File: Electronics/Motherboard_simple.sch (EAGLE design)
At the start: 27 parts, among them U2 USD-SOCKETNEW

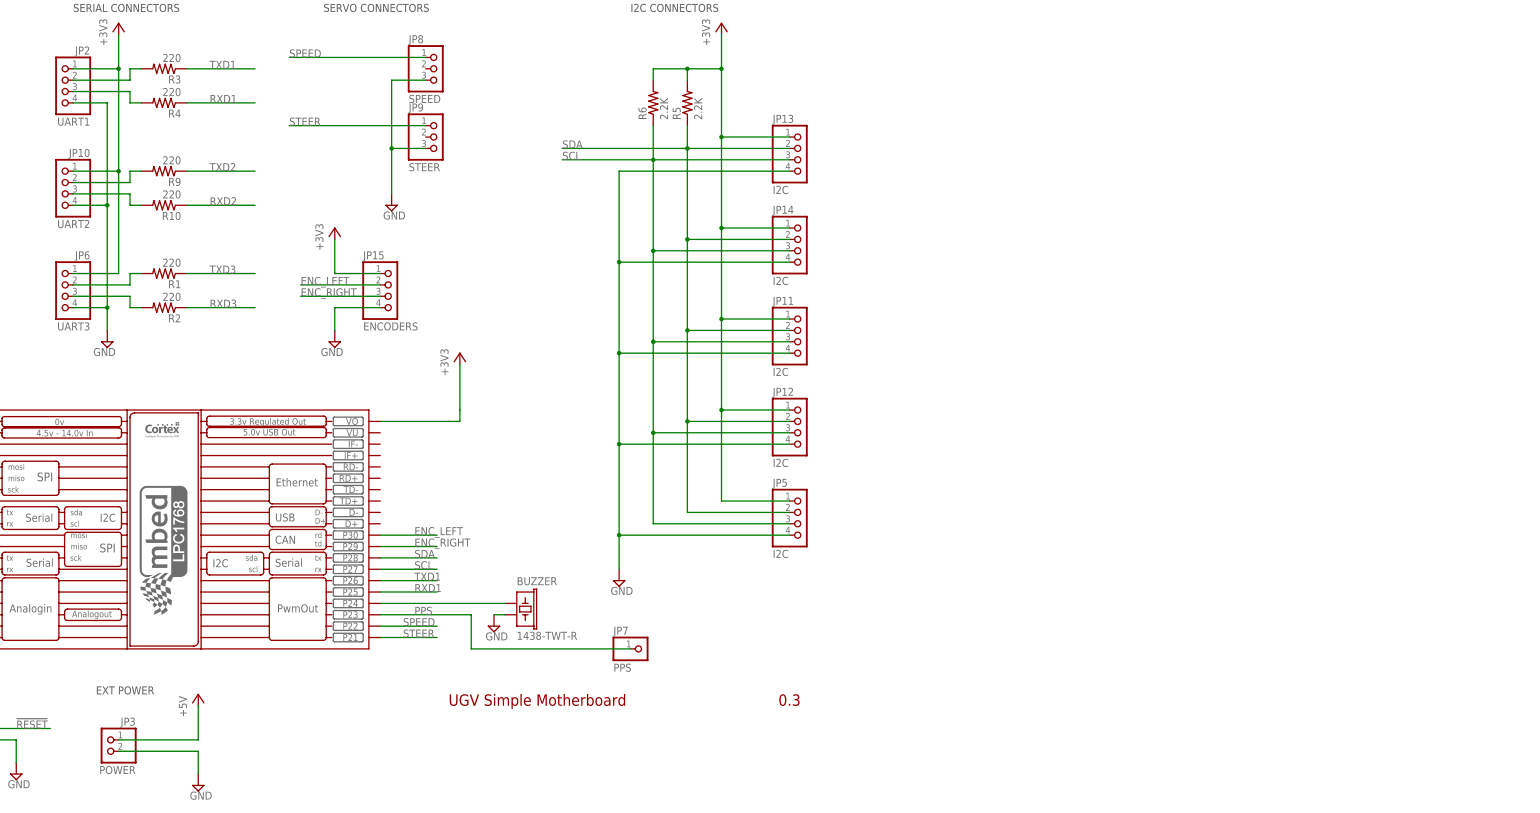
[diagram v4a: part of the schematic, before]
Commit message: Major revision for through hole, onboard encoder interface.
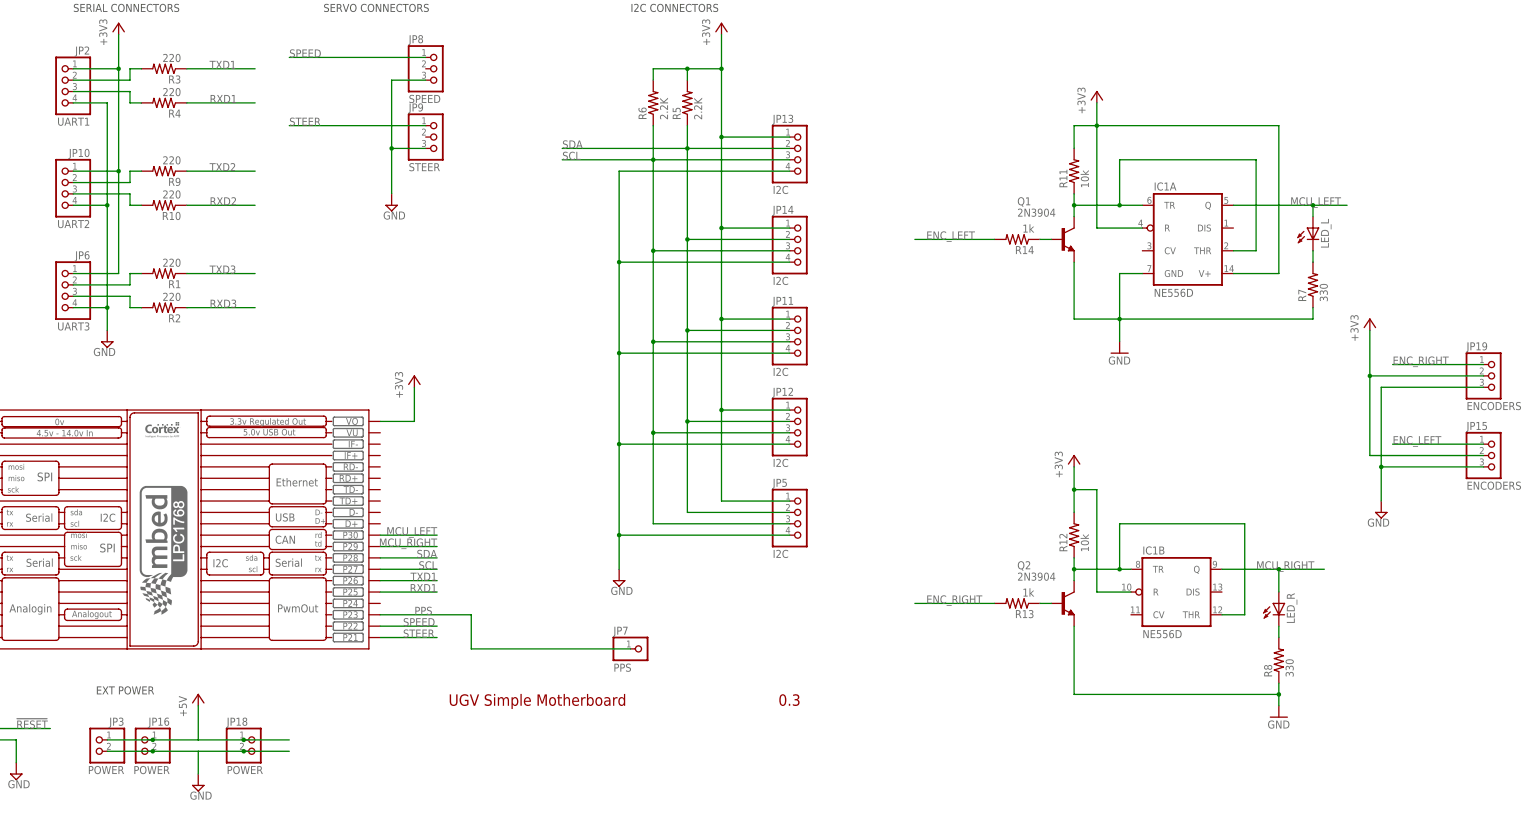
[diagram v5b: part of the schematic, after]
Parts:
- removed BUZZER: 1438-TWT-R, mes_buzzers:BUZZER-AT-1438-TWT-R
- added IC1: NE556D, linear:NE556D
- added JP16, JP18: POWER, pinhead-2:PINHD-1X02_2.54-S
- added JP19: ENCODERS, pinhead-2:PINHD-1X03_2.54-S
- added LED_L, LED_R: (no value), led:LED3MM
- added Q1, Q2: 2N3904, mes_transistors:2N3904INLINE
- added R11, R12: 10k, rcl:R-US_0204/5
- added R13, R14: 1k, rcl:R-US_0204/5
- added R7, R8: 330, rcl:R-US_0204/5
- JP15: device pinhead-2:PINHD-1X04_2.54-S -> pinhead-2:PINHD-1X03_2.54-S
- JP3: device pinhead-2:PINHD-1X02_2.54-90°-S -> pinhead-2:PINHD-1X02_2.54-S
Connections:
- new net MCU_LEFT: IC1A.Q, LED_L.A, MBED.P30
- new net MCU_RIGHT: IC1B.Q, LED_R.A, MBED.P29
- new net N$11: IC1B.THR, IC1B.TR, Q2.C, R12.1
- new net N$13: Q2.B, R13.1
- new net N$14: Q1.B, R14.1
- new net N$3: LED_L.C, R7.2
- new net N$4: LED_R.C, R8.2
- net +3V3: now also IC1A.R, IC1A.V+, IC1B.R, JP15.2, JP19.2, R11.2, R12.2; no longer JP15.1
- net +5V: now also JP16.1, JP18.1
- net ENC_LEFT: now also JP15.1, R14.2; no longer JP15.2, MBED.P30
- net ENC_RIGHT: now also JP19.1, R13.2; no longer JP15.3, MBED.P29
- net GND: now also IC1A.GND, JP15.3, JP16.2, JP18.2, JP19.3, Q1.E, Q2.E, R7.1, R8.1; no longer BUZZER.2, JP15.4
- net N$12: now also IC1A.THR, IC1A.TR, Q1.C, R11.1; no longer BUZZER.1, MBED.P24
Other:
- moved on the sheet: JP3

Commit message: Major revision, added RC takeover switch circuitry. Moved encoder interface.
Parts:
- added C1, C2: 104, rcl:C-US050-025X075
- added IC2, IC3: 741G3157DBVR, 74xx-little-us:741G3157DBVR
- added IC4: TINY25, avr-7:TINY138P3
- added JP20: I2C, pinhead-2:PINHD-1X04_2.54-S
- added JP21: RXE, pinhead-2:PINHD-1X03_2.54-S
- added JP22: RXS, pinhead-2:PINHD-1X03_2.54-S
- added R15: 10k, rcl:R-US_0204/5
- JP8: value SPEED -> ESC
- JP9: value STEER -> SRV
- Q1, Q2: device mes_transistors:2N3904INLINE -> mes_transistors:2N3904
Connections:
- removed net SPEED: JP8.1, MBED.P22
- removed net STEER: JP9.1, MBED.P21
- new net BEC: JP21.2, JP22.2, JP8.2, JP9.2
- new net ESC: IC2G$1.X, JP8.1
- new net MCUESC: IC2G$1.B, MBED.P22
- new net MCUSRV: IC3G$1.B, MBED.P21
- new net N$15: IC4.(RESET)PB5, R15.1
- new net N$25: IC2G$1.!A!/B, IC3G$1.!A!/B, IC4.(ADC3)PB3
- new net RXESC: IC2G$1.A, IC4.(MOSI)PB0, JP21.1, MBED.P24
- new net RXSRV: IC3G$1.A, JP22.1, MBED.P23
- new net SRV: IC3G$1.X, JP9.1
- net +3V3: now also C1.1, C2.1, IC4.VCC, JP20.1, R15.2
- net GND: now also C1.2, C2.2, IC4.GND, JP20.4, JP21.3, JP22.3
- net PPS: no longer MBED.P23
- net SCL: now also JP20.3
- net SDA: now also JP20.2
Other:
- note added: "0.5"
- note added: "Data Bus Baseboard"
- note removed: "0.3"
- note removed: "SERVO CONNECTORS"
- note removed: "UGV Simple Motherboard"
- moved on the sheet: IC1A, IC1B, JP15, JP19, JP7, JP8, JP9, LED_L, LED_R, Q1, Q2, R11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

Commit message: Routing tweaks. Added 5V header. Added AVRISP hdr for Tiny
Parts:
- added J1: AVRISP, ads4:AVRISP6
- added JP23: POWER, pinhead-2:PINHD-1X02_2.54-S
- added SJ1, SJ2: (no value), SparkFun:SOLDERJUMPER_2WAYS
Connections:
- removed net N$15: IC4.(RESET)PB5, R15.1
- new net !TRST: IC4.(RESET)PB5, J1.!RESET, R15.1
- new net MISO: IC4.(MISO)PB1, J1.MISO
- new net N$18: JP10.1, SJ1.2
- new net N$19: JP6.1, SJ2.2
- new net SCK: IC4.(SCK)PB2, J1.SCK
- net +3V3: now also J1.VCC, SJ1.3, SJ2.3; no longer JP10.1, JP6.1
- net +5V: now also JP23.1, SJ1.1, SJ2.1
- net GND: now also J1.GND, JP23.2
- net PPS: now also MBED.P11
- net RXESC: now also J1.MOSI
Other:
- note added: "ENCODER INTERFACE"
- note added: "OUTPUT"
- note added: "RC TAKEOVER SWITCH"
- note added: "RX INPUT"
- moved on the sheet: C1, C2, IC1A, IC1B, IC2, IC3, IC4, JP11, JP12, JP13, JP14, JP15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

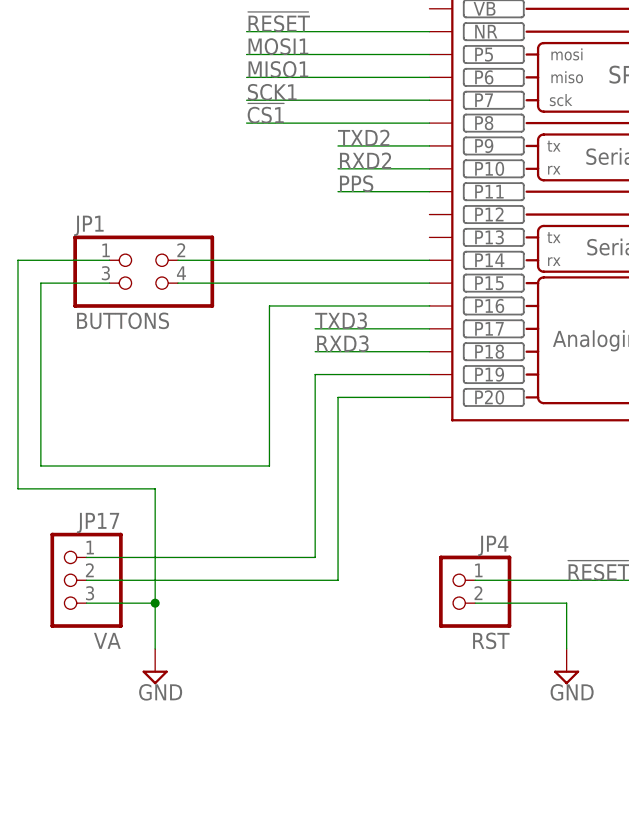
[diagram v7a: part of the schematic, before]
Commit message: Layout tweaks
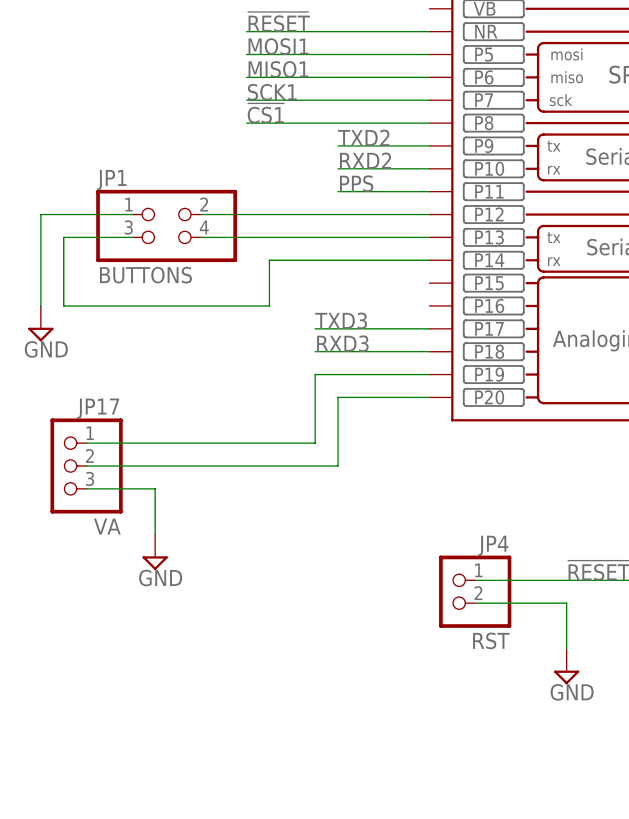
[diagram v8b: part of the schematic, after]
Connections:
- net N$5: now also JP1.4, MBED.P13; no longer JP1.2, MBED.P14
- net N$7: now also JP1.2, MBED.P12; no longer JP1.4, MBED.P15
- net N$8: now also MBED.P14; no longer MBED.P16
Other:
- moved on the sheet: JP1, JP17
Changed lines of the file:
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@@
 <attribute name="OC_NEWARK" value="unknown"/>
 </part>
+<part name="SUPPLY10" library="supply2" deviceset="GND" device=""/>
 </parts>
 <sheets>
@@
 <attribute name="MPN" x="398.78" y="88.9" size="1.778" layer="96" rot="MR0" display="off"/>
 </instance>
-<instance part="SUPPLY9" gate="GND" x="17.78" y="10.16"/>
+<instance part="SUPPLY9" gate="GND" x="17.78" y="22.86"/>
 <instance part="R1" gate="G$1" x="96.52" y="121.92" rot="R180">
 <attribute name="OC_NEWARK" x="96.52" y="121.92" size="1.778" layer="96" display="off"/>
@@
 <attribute name="MPN" x="96.52" y="160.02" size="1.778" layer="96" display="off"/>
 </instance>
-<instance part="JP17" gate="A" x="7.62" y="20.32" rot="MR0">
-<attribute name="OC_NEWARK" x="7.62" y="20.32" size="1.778" layer="96" display="off"/>
-<attribute name="MF" x="7.62" y="20.32" size="1.778" layer="96" display="off"/>
-<attribute name="MPN" x="7.62" y="20.32" size="1.778" layer="96" display="off"/>
+<instance part="JP17" gate="A" x="7.62" y="33.02" rot="MR0">
+<attribute name="OC_NEWARK" x="7.62" y="33.02" size="1.778" layer="96" display="off"/>
+<attribute name="MF" x="7.62" y="33.02" size="1.778" layer="96" display="off"/>
+<attribute name="MPN" x="7.62" y="33.02" size="1.778" layer="96" display="off"/>
 </instance>
 <instance part="JP5" gate="A" x="213.36" y="66.04">
@@
 <attribute name="MPN" x="213.36" y="66.04" size="1.778" layer="96" display="off"/>
 </instance>
-<instance part="JP1" gate="A" x="17.78" y="53.34"/>
+<instance part="JP1" gate="A" x="20.32" y="58.42"/>
 <instance part="JP7" gate="A" x="73.66" y="101.6" rot="MR0"/>
 <instance part="JP10" gate="A" x="73.66" y="139.7" rot="MR0">
@@
 <attribute name="MPN" x="116.84" y="15.24" size="1.778" layer="96" rot="MR0" display="off"/>
 </instance>
+<instance part="SUPPLY10" gate="GND" x="5.08" y="48.26"/>
 </instances>
 <busses>
@@
 </segment>
 <segment>
-<wire x1="17.78" y1="17.78" x2="17.78" y2="12.7" width="0.1524" layer="91"/>
+<pinref part="JP1" gate="A" pin="1"/>
+<wire x1="5.08" y1="60.96" x2="15.24" y2="60.96" width="0.1524" layer="91"/>
+<wire x1="5.08" y1="50.8" x2="5.08" y2="60.96" width="0.1524" layer="91"/>
+<pinref part="SUPPLY10" gate="GND" pin="GND"/>
+</segment>
+<segment>
+<wire x1="17.78" y1="30.48" x2="17.78" y2="25.4" width="0.1524" layer="91"/>
 <pinref part="SUPPLY9" gate="GND" pin="GND"/>
-<wire x1="17.78" y1="17.78" x2="10.16" y2="17.78" width="0.1524" layer="91"/>
-<wire x1="2.54" y1="30.48" x2="17.78" y2="30.48" width="0.1524" layer="91"/>
-<wire x1="17.78" y1="17.78" x2="17.78" y2="30.48" width="0.1524" layer="91"/>
-<junction x="17.78" y="17.78"/>
+<wire x1="17.78" y1="30.48" x2="10.16" y2="30.48" width="0.1524" layer="91"/>
 <pinref part="JP17" gate="A" pin="3"/>
-<wire x1="2.54" y1="30.48" x2="2.54" y2="55.88" width="0.1524" layer="91"/>
-<pinref part="JP1" gate="A" pin="1"/>
-<wire x1="2.54" y1="55.88" x2="12.7" y2="55.88" width="0.1524" layer="91"/>
 </segment>
 <segment>
@@
 <segment>
 <wire x1="48.26" y1="40.64" x2="38.1" y2="40.64" width="0.1524" layer="91"/>
-<wire x1="38.1" y1="40.64" x2="38.1" y2="20.32" width="0.1524" layer="91"/>
-<wire x1="38.1" y1="20.32" x2="10.16" y2="20.32" width="0.1524" layer="91"/>
+<wire x1="38.1" y1="40.64" x2="38.1" y2="33.02" width="0.1524" layer="91"/>
+<wire x1="38.1" y1="33.02" x2="10.16" y2="33.02" width="0.1524" layer="91"/>
 <pinref part="MBED" gate="KIT" pin="P20"/>
 <pinref part="JP17" gate="A" pin="2"/>
@@
 <net name="N$6" class="0">
 <segment>
-<wire x1="35.56" y1="22.86" x2="35.56" y2="43.18" width="0.1524" layer="91"/>
+<wire x1="35.56" y1="35.56" x2="35.56" y2="43.18" width="0.1524" layer="91"/>
 <wire x1="35.56" y1="43.18" x2="48.26" y2="43.18" width="0.1524" layer="91"/>
 <pinref part="MBED" gate="KIT" pin="P19"/>
-<wire x1="35.56" y1="22.86" x2="10.16" y2="22.86" width="0.1524" layer="91"/>
+<wire x1="35.56" y1="35.56" x2="10.16" y2="35.56" width="0.1524" layer="91"/>
 <pinref part="JP17" gate="A" pin="1"/>
 </segment>
@@
 </segment>
 </net>
-<net name="N$5" class="0">
-<segment>
+<net name="N$8" class="0">
+<segment>
+<wire x1="30.48" y1="50.8" x2="7.62" y2="50.8" width="0.1524" layer="91"/>
+<wire x1="7.62" y1="50.8" x2="7.62" y2="58.42" width="0.1524" layer="91"/>
+<pinref part="JP1" gate="A" pin="3"/>
+<wire x1="7.62" y1="58.42" x2="15.24" y2="58.42" width="0.1524" layer="91"/>
+<wire x1="30.48" y1="50.8" x2="30.48" y2="55.88" width="0.1524" layer="91"/>
 <pinref part="MBED" gate="KIT" pin="P14"/>
-<wire x1="20.32" y1="55.88" x2="48.26" y2="55.88" width="0.1524" layer="91"/>
-<pinref part="JP1" gate="A" pin="2"/>
-</segment>
-</net>
-<net name="N$7" class="0">
-<segment>
-<pinref part="MBED" gate="KIT" pin="P15"/>
-<wire x1="48.26" y1="53.34" x2="20.32" y2="53.34" width="0.1524" layer="91"/>
-<pinref part="JP1" gate="A" pin="4"/>
-</segment>
-</net>
-<net name="N$8" class="0">
-<segment>
-<pinref part="MBED" gate="KIT" pin="P16"/>
-<wire x1="48.26" y1="50.8" x2="30.48" y2="50.8" width="0.1524" layer="91"/>
-<wire x1="30.48" y1="50.8" x2="30.48" y2="33.02" width="0.1524" layer="91"/>
-<wire x1="30.48" y1="33.02" x2="5.08" y2="33.02" width="0.1524" layer="91"/>
-<wire x1="5.08" y1="33.02" x2="5.08" y2="53.34" width="0.1524" layer="91"/>
-<pinref part="JP1" gate="A" pin="3"/>
-<wire x1="5.08" y1="53.34" x2="12.7" y2="53.34" width="0.1524" layer="91"/>
+<wire x1="30.48" y1="55.88" x2="48.26" y2="55.88" width="0.1524" layer="91"/>
 </segment>
 </net>
@@
 </segment>
 </net>
+<net name="N$5" class="0">
+<segment>
+<pinref part="MBED" gate="KIT" pin="P13"/>
+<pinref part="JP1" gate="A" pin="4"/>
+<wire x1="48.26" y1="58.42" x2="22.86" y2="58.42" width="0.1524" layer="91"/>
+</segment>
+</net>
+<net name="N$7" class="0">
+<segment>
+<pinref part="MBED" gate="KIT" pin="P12"/>
+<pinref part="JP1" gate="A" pin="2"/>
+<wire x1="48.26" y1="60.96" x2="22.86" y2="60.96" width="0.1524" layer="91"/>
+</segment>
+</net>
